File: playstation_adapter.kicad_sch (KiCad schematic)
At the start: 10 parts, among them J1 Conn_01x03, J2 Conn_01x13, J3 GT-USB-7047C, U1 XC6206P332MR, U2 SRV05-4

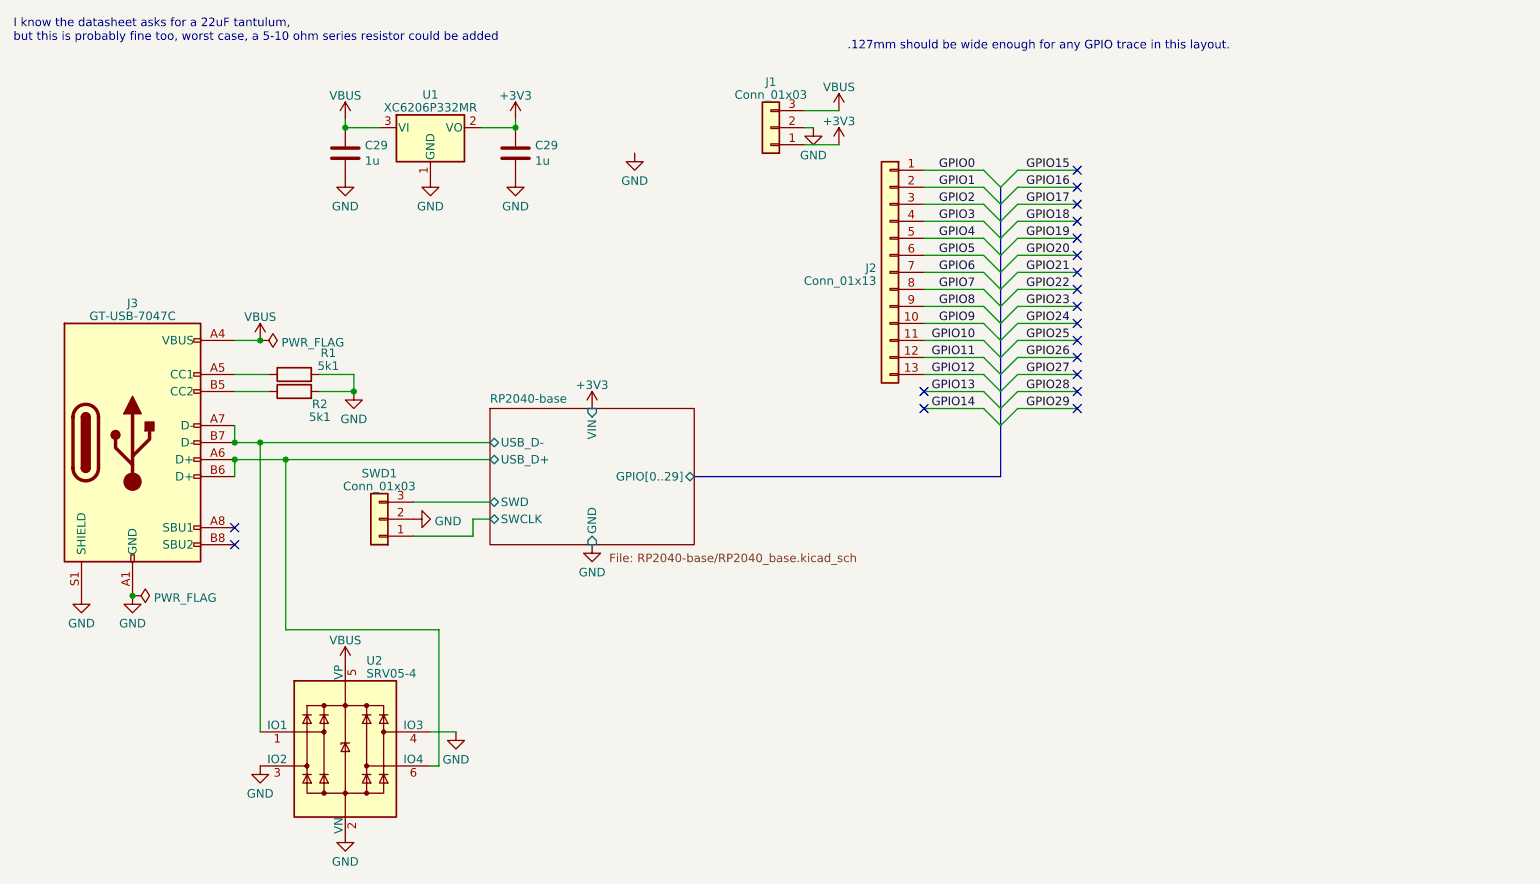
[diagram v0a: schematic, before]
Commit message: Modified example pcb to playstation adapter pcb
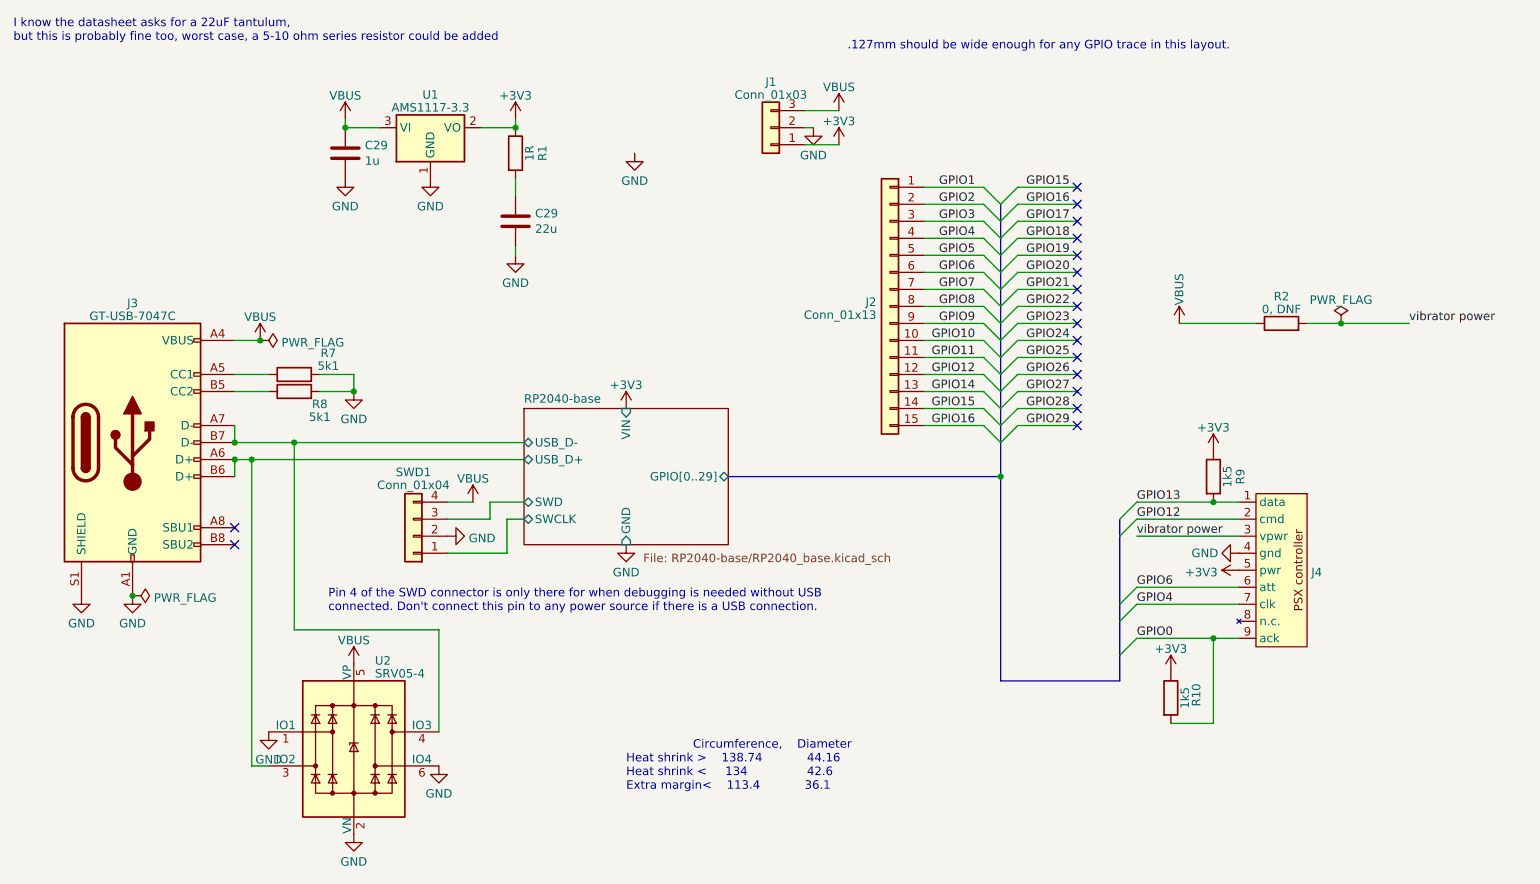
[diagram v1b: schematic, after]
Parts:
- removed J2: Conn_01x13, Connector_PinHeader_2.54mm:PinHeader_1x13_P2.54mm_Vertical, symbol Connector_Generic:Conn_01x13
- removed SWD1: Conn_01x03, Connector_PinHeader_2.54mm:PinHeader_1x03_P2.54mm_Vertical, symbol Connector_Generic:Conn_01x03
- removed U1: XC6206P332MR, footprints:SOT-23-3_flipped_for_jlcpcb, symbol Regulator_Linear:XC6206PxxxMR
- added J2: Conn_01x13, footprints:PinHeader_1x15_P2.54mm_Vertical_no_courtyard, symbol Connector_Generic:Conn_01x15
- added J4: ~, footprints:PSX port, symbol playstation_adapter:PSX_port
- added R1: 1R, Resistor_SMD:R_0603_1608Metric, symbol Device:R
- added R10, R9: 1k5, Resistor_SMD:R_0402_1005Metric, symbol Device:R
- added R2: 0, DNF, Resistor_SMD:R_0805_2012Metric, symbol Device:R
- added SWD1: Conn_01x04, footprints:REDFIT 4 pin, symbol Connector_Generic:Conn_01x04
- added U1: AMS1117-3.3, footprints:SOT-223-3_TabPin2_flipped_for_jlcpcb, symbol Regulator_Linear:AMS1117-3.3
- C29: value 1u -> 22u
- renumbered R1 to R7, R2 to R8
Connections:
- net +3V3: now also J4.5 (pwr), R1.1, R10.1, R9.1, U1.2 (VO); no longer C29.1
- net GND: now also U2.1 (IO1), U2.6 (IO4), J4.4 (gnd), SWD1.2 (Pin_2), U1.1 (GND); no longer U2.3 (IO2), U2.4 (IO3)
- net GPIO0: now also J4.9 (ack), R10.2
- net GPIO1: now also J2.1 (Pin_1)
- net GPIO10: now also J2.10 (Pin_10)
- net GPIO11: now also J2.11 (Pin_11)
- net GPIO12: now also J2.12 (Pin_12), J4.2 (cmd)
- net GPIO13: now also J4.1 (data), R9.2
- net GPIO14: now also J2.13 (Pin_13)
- net GPIO15: now also J2.14 (Pin_14)
- net GPIO16: now also J2.15 (Pin_15)
- net GPIO2: now also J2.2 (Pin_2)
- net GPIO3: now also J2.3 (Pin_3)
- net GPIO4: now also J2.4 (Pin_4), J4.7 (clk)
- net GPIO5: now also J2.5 (Pin_5)
- net GPIO6: now also J2.6 (Pin_6), J4.6 (att)
- net GPIO7: now also J2.7 (Pin_7)
- net GPIO8: now also J2.8 (Pin_8)
- net GPIO9: now also J2.9 (Pin_9)
- net RP2040-base/SWCLK: now also SWD1.1 (Pin_1)
- net RP2040-base/SWD: now also SWD1.3 (Pin_3)
- net RP2040-base/USB_D+: now also U2.3 (IO2); no longer U2.6 (IO4)
- net RP2040-base/USB_D-: now also U2.4 (IO3); no longer U2.1 (IO1)
- net VBUS: now also R2.1, SWD1.4 (Pin_4), U1.3 (VI)
- new net: C29.1, R1.2
- new net vibrator power: J4.3 (vpwr), R2.2
- no-connect marks 19 -> 17
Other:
- note added: "Circumference, Diameter Heat shrink > 138.74 44.16 Heat shrink < 134 42.6 Extra margin< 113.4 36.1"
- note added: "Pin 4 of the SWD connector is only there for when debugging is needed without USB connected. Don't connect this pin to any power source if there is a USB connection."
- company: https://github.com/TT-392/RP2040-base-example -> git@github.com:TT-392/playstation_adapter.git
- title: RP2040-base example -> playstation adapter
- moved on the sheet: U2
